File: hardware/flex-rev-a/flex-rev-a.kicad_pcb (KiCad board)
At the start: 2 copper layers, 72 x 20 mm, 51 parts, among them J601 Dock pads, SW201 button DNP, U1 ISP2454-LX, U201 nPM1304-QEAA, U401 LIS2DW12TR, U501 DRV2605LDGSR

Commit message: Lengthen both flex islands by 4 mm for a 22 x 40 mm pod
The antenna shadow on island B mirrors island A's far end across the fold,
so island A grows with island B: A is now x 96-132 (36 x 18 mm) with the
ISP2454 moved to its new far end, B is x 140-176 (36 x 20 mm). The shadow
rule area moves to x 171-176 and the 30 mm cell bay (x 140.5-170.5) ends
0.5 mm before it. Stiffener map, keep-out drawings, fab notes, layout PDF
and README pod size updated. Placement otherwise unchanged; DRC still has
no shorts, clearance, courtyard or keep-out errors (unrouted nets and
silkscreen only).

Co-Authored-By: Claude Opus 5.5 <noreply@anthropic.com>
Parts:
- moved U1 4.00 mm to (101.0, 109.0)
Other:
- board size 72 x 20 mm -> 80 x 20 mm
- board text added: "Antenna shadow after fold (x 171-176): no copper, no cell, no LRA"
- board text added: "WakeBand flex rev A, layout hand-off (step 8). Unfolded view, all parts top side. Pod about 22 x 40 mm. Island A 36 x 18, island B 36 x 20; the 30 mm cell bay ends 0.5 mm before the antenna shadow. Stackup: 2-layer adhesiveless PI 25 um, 18 um Cu, coverlay, ENIG, about 0.12 mm. Stiffeners on the bottom (User.2): FR4 0.4 under island A and the LRA pad, PI 0.2 behind the dock pads. No steel stiffen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"
- board text removed: "Antenna shadow after fold: no copper, no cell, no LRA"
- board text removed: "WakeBand flex rev A, layout hand-off (step 8). Unfolded view, all parts top side. Stackup: 2-layer adhesiveless PI 25 um, 18 um Cu, coverlay, ENIG, about 0.12 mm. Stiffeners on the bottom (User.2): FR4 0.4 under island A and the LRA pad, PI 0.2 behind the dock pads. No steel stiffeners. Bend zone (User.3): no vias or parts, R >= 1.2 mm. Vias only on stiffened areas, >= 0.5 mm from a stiffener edg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"

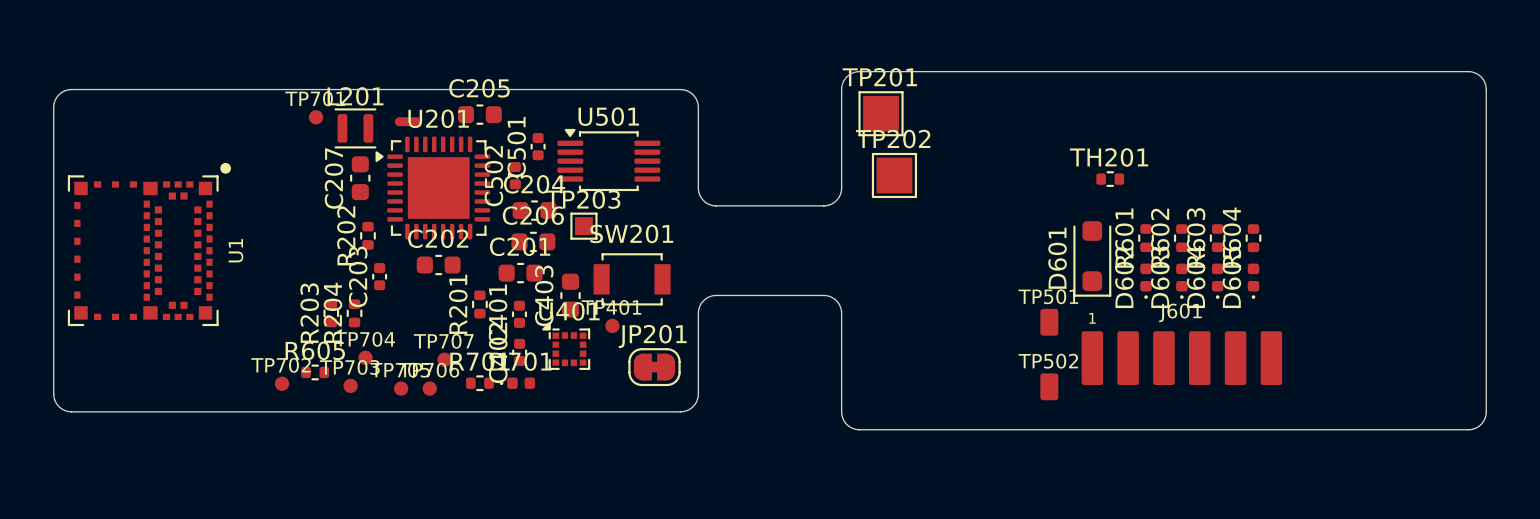
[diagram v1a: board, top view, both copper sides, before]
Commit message: Route flex rev A (partial): DRC 0 errors, 3 nets open
- Freerouting 1.9.0 route of all nets, GND included; GND pours on island A
  (both layers), island B (top) and hatched top in the neck; ISP2454 pads
  8/24 tied to 7/25; teardrops enabled on all pads and vias.
- R601-R604 moved to island A next to the neck; neck widened 5 -> 7 mm.
- Net classes (power 0.3, motor 0.25, VDD_2V0 0.2, GND 0.2, signals
  0.12 mm, clearance 0.13), no-via areas off the stiffeners, edge bands.
- DRC exclusions for the 6 ISP2454 GND pads left unconnected on purpose.
- Open: PAD_SWDIO (R602), VBUSOUT (C206), NTC (U201-TH201). Warnings are
  silkscreen only. Pad nets match the schematic; ERC still 0/0.

Co-Authored-By: Claude Opus 5.5 <noreply@anthropic.com>
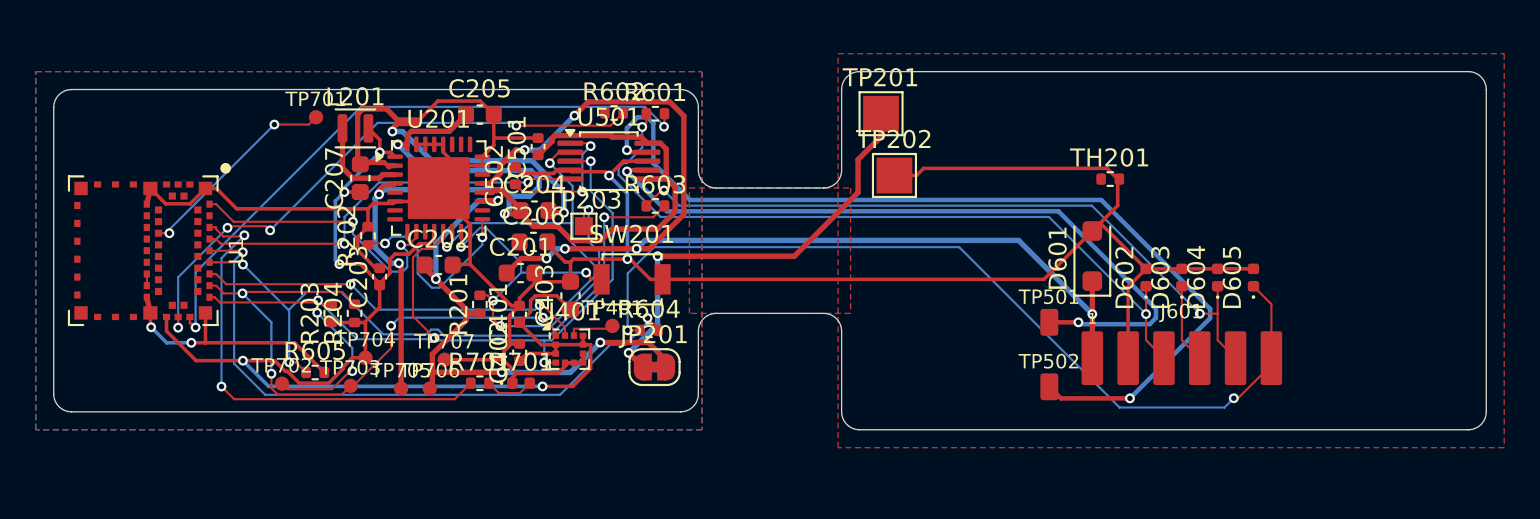
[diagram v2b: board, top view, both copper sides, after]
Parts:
- moved R604 34.1 mm to (129.2, 113.5), turned to 0 degrees
- moved R602 32.5 mm to (127.3, 101.3), turned to 0 degrees
- moved R603 31.5 mm to (129.6, 106.5), turned to 0 degrees
- moved R601 28.3 mm to (129.6, 101.3), turned to 0 degrees
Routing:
- net GND: track 0.00 -> 159.6 mm, vias 0 -> 4
- net VDD_2V0: track 0.00 -> 72.2 mm, vias 0 -> 5
- net VSYS: track 0.00 -> 64.1 mm, vias 0 -> 4
- net VIN: track 0.00 -> 62.1 mm, vias 0 -> 6
- net I2C_SCL: track 0.00 -> 54.9 mm, vias 0 -> 6
- net I2C_SDA: track 0.00 -> 52.6 mm, vias 0 -> 6
- net LRA_N: track 0.00 -> 52.6 mm, vias 0 -> 2
- net PAD_TX: track 0.00 -> 49.9 mm, vias 0 -> 2
- net PAD_SWDCLK: track 0.00 -> 41.3 mm, vias 0 -> 2
- net LRA_P: track 0.00 -> 40.5 mm, vias 0 -> 2
- net PAD_RX: track 0.00 -> 39.5 mm, vias 0 -> 2
- net UART_RX: track 0.00 -> 37.4 mm, vias 0 -> 3
- net SWDCLK: track 0.00 -> 35.1 mm, vias 0 -> 2
- net UART_TX: track 0.00 -> 35.0 mm, vias 0 -> 2
- net SWDIO: track 0.00 -> 32.4 mm, vias 0 -> 4
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- added copper zone on B.Cu, net GND
- added copper zone on F.Cu, net GND
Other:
- outline, holes or cut-outs redrawn
- board text added: "BEND (7 mm neck): no vias/parts, traces 90 deg to fold, hatched GND"
- board text removed: "BEND: no vias/parts, curved traces 90 deg to fold, hatched GND"

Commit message: Complete flex rev A routing: DRC 0 errors, 0 warnings, 0 unconnected
- Placement for routing: U501 group to the lower right of island A, U401
  group next to the module, PMIC caps regrouped so U201's power pins have a
  clear path to the neck (R601-R604 already on island A, neck 7 mm).
- Freerouting 1.9.0 for the bulk; scripted grid router for the last VSYS
  link (0.15 mm at the QFN pin) and two GND links joining module pads
  25 and 31 to the main ground.
- Neck: no vias, straight traces perpendicular to the fold, top and bottom
  traces staggered (45-degree jogs at the neck ends), hatched top GND.
- GND: solid top pours on both islands, hatched in the neck; no bottom
  pour (it only left floating slivers). No copper in the antenna keep-outs.
- ISP2454 outer-row pads only: nRESET (inner pad 13) left unrouted with
  TP701 kept; reserved GND pads 12-18, 21, 23 unconnected. 7 DRC
  exclusions with comments in the .kicad_pro.
- Teardrops enabled on all pads/vias (generated when zones are refilled in
  KiCad); reference designators moved to F.Fab, silk overlaps cleared.
- Layout PDF replotted, README routing section updated. Pad nets match the
  schematic; ERC 0/0.

Co-Authored-By: Claude Opus 5.5 <noreply@anthropic.com>
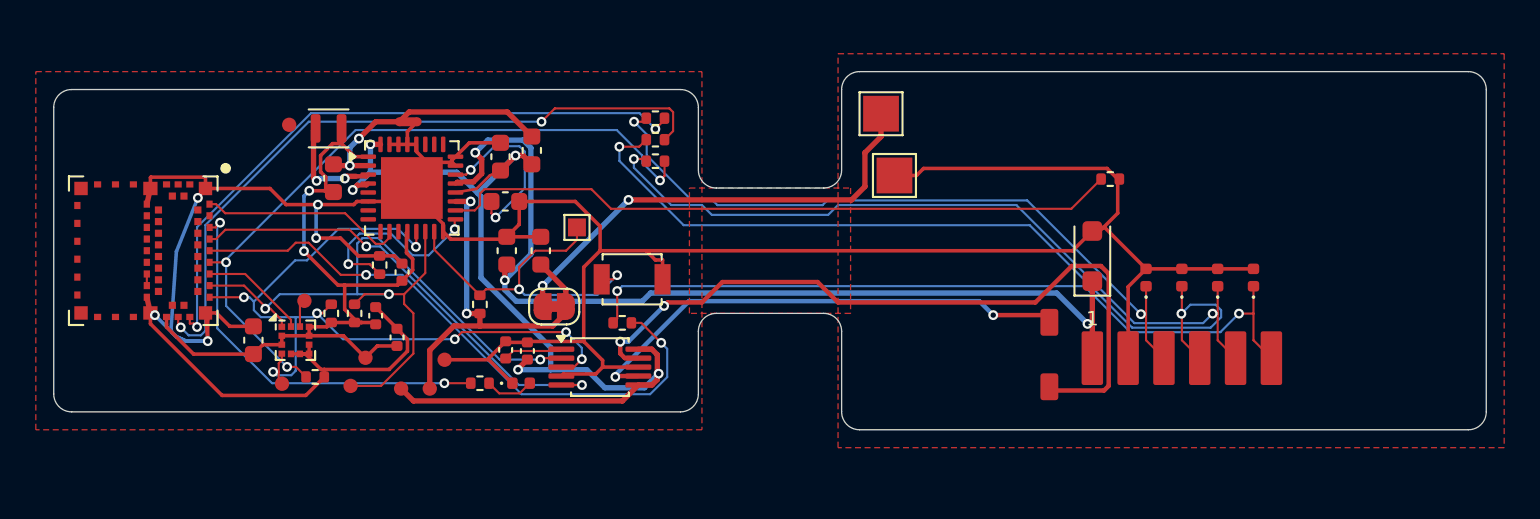
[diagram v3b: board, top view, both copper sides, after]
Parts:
- moved C403 17.9 mm to (107.2, 114.0)
- moved TP401 17.3 mm to (110.0, 111.8)
- moved U401 15.3 mm to (109.5, 114.0)
- moved U501 11.5 mm to (126.5, 115.5)
- moved C501 11.4 mm to (122.5, 114.6)
- moved C502 9.74 mm to (121.2, 114.5)
- moved C401 8.03 mm to (114.0, 112.6)
- moved C402 6.90 mm to (115.2, 113.8)
- moved JP201 6.54 mm to (124.0, 112.1)
- moved C202 5.76 mm to (123.2, 109.0), turned to 90 degrees
- moved C204 3.36 mm to (122.7, 103.4), turned to 90 degrees
- moved C206 2.75 mm to (121.2, 106.2)
- moved R602 2.75 mm to (129.6, 102.8)
- moved C205 2.62 mm to (121.0, 103.8), turned to 90 degrees
- moved R603 2.50 mm to (129.6, 104.0)
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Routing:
- net PAD_SWDIO: track 4.43 -> 47.6 mm, vias 0 -> 2
- net NTC: track 0.00 -> 38.1 mm
- net VDD_2V0: track 72.2 -> 43.1 mm, vias 5 -> 2
- net GND: track 159.6 -> 183.7 mm, vias 4 -> 5
- net ACC_INT1: track 21.8 -> 5.99 mm, vias 2 -> 0
- net LRA_P: track 40.5 -> 27.8 mm
- net nRESET: track 11.6 -> 0.00 mm, vias 2 -> 0
- net LRA_N: track 52.6 -> 41.7 mm
- net I2C_SCL: track 54.9 -> 44.5 mm, vias 6 -> 3
- net VBUSOUT: track 0.00 -> 9.99 mm, vias 0 -> 2
- net VBAT: track 31.4 -> 22.5 mm, vias 4 -> 2
- net I2C_SDA: track 52.6 -> 44.3 mm, vias 6 -> 7
- net VIN: track 62.1 -> 54.3 mm, vias 6 -> 3
- net SHPHLD: track 27.1 -> 19.8 mm, vias 5 -> 2
- net PVSS1: track 21.4 -> 14.5 mm
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- removed copper zone on B.Cu, net GND

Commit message: Fix fold orientation: cell and LRA pads to island B's B side; fab package
Island B folds under island A, so its B side is the inner face where the
cell and LRA sit.
- TP201/TP202 (cell tabs, neck end) and TP501/TP502 (LRA leads, just
  outside the LRA stiffener) moved to B.Cu/B.Mask, clear of stiffeners.
- BATT_P, LRA+, LRA- and the TP202 GND link rerouted to them; the LRA pair
  moved up on F.Cu in the neck so no trace sits over another at the fold.
- All SMT parts stay on F (single-sided assembly); NTC stays on F.
- Fold/assembly orientation note added to the fab notes layer and README.
- fab/: Gerbers (copper, mask, paste, silk, edge, bottom stiffener, bend
  zone, antenna keep-out, notes, fab) exported with --check-zones so
  teardrops are generated; Excellon drill + maps; JLCPCB BOM and top CPL
  (31 fitted parts); everything also zipped.
- DRC 0 violations / 0 unconnected / 0 footprint errors (documented
  exclusions for the reserved ISP2454 pads and nRESET); pad nets match the
  schematic; ERC 0/0.

Co-Authored-By: Claude Opus 5.5 <noreply@anthropic.com>
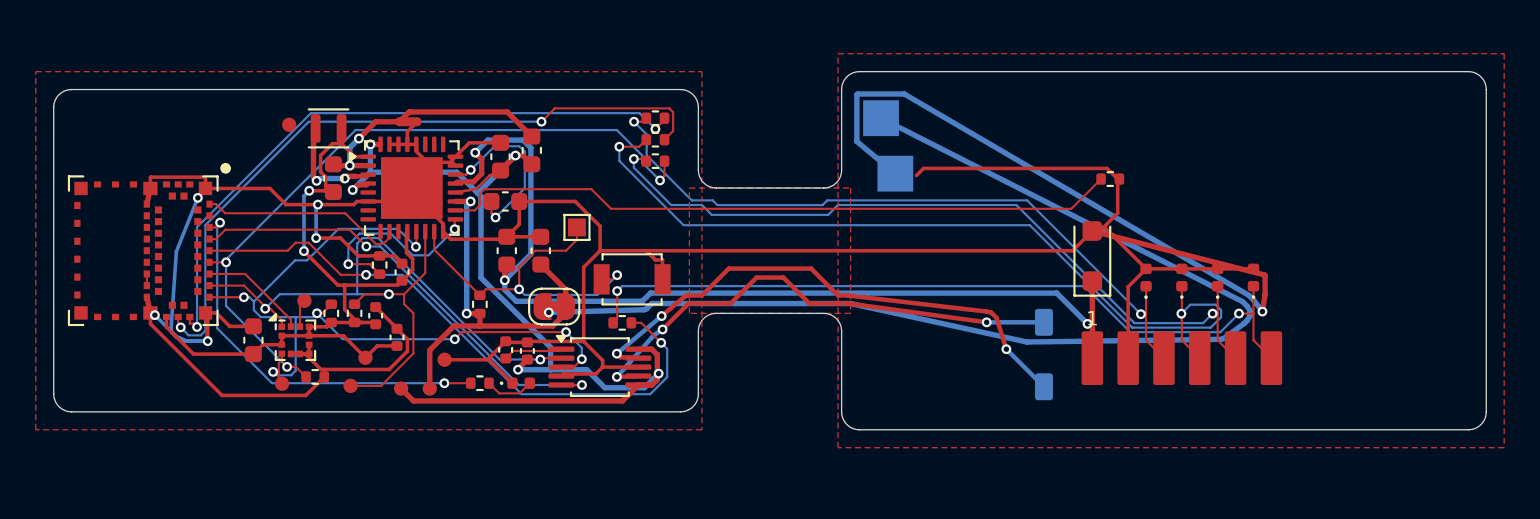
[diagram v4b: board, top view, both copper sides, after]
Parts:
- TP201, TP202, TP501, TP502: moved to B.Cu
- moved TP501 0.30 mm to (151.3, 113.0), turned to 180 degrees
- moved TP502 0.30 mm to (151.3, 116.6), turned to 180 degrees
- moved TP201 0.25 mm to (142.2, 101.6), turned to 180 degrees
- moved TP202 0.11 mm to (143.0, 104.7), turned to 180 degrees
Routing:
- net GND: track 183.7 -> 226.0 mm, vias 5 -> 6
- net BATT_P: track 25.9 -> 63.6 mm, vias 2 -> 1
- net LRA_N: track 41.7 -> 29.9 mm, vias 2 -> 3
- net LRA_P: track 27.8 -> 28.1 mm, vias 2 -> 3
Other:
- board text added: "FOLD / ASSEMBLY ORIENTATION (fold line x = 136, island B folds UNDER island A): - Island A F side (all SMT parts) faces UP, away from the wrist. - Island B F side faces DOWN to the case floor: dock pads J601 face the dock. - Cell and LRA mount on island B's B side (inner face, between the islands): cell tabs solder to TP201 (+) / TP202 (-), LRA leads to TP501 (+) / TP502 (-), all on B.Cu; LRA tap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"

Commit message: Rework flex layout per layout review: 23.5 x 40 pod, straight neck lanes
- Islands widened to 21.5 mm (pod about 23.5 x 40 mm); island B across the
  width: 0.3 edge, 12 mm cell bay, 0.5 gap, 8 mm LRA strip, 0.7 edge, so the
  LRA no longer overlaps the cell.
- Neck widened to 9 mm; every trace in it is one straight locked lane along
  x (7 on F.Cu, 4 on B.Cu), no vias, >= 0.5 mm in y between F and B lanes.
- Cell tabs TP201/TP202 and LRA leads TP501/TP502 on island B's B side,
  outside the cell bay, 0.5 mm clearance to other nets, mask +0.1 mm;
  battery +/- run 0.4 mm straight to their lanes (no vias on island B), 4
  battery-path vias on island A each doubled.
- One merged FR4 0.4 stiffener under island B's LRA/dock strip (TVS, NTC,
  dock pads on it) with windows around the B-side pads; antenna keep-out
  widened to the full island width.
- No vias on SMD pads (except 4 intended vias in the nPM1304 exposed pad);
  nRESET left unrouted (inner pad 13); ANT_LINK a 0.65 mm trace.
- GND: top pour on both islands, bottom pour on island A, hatched top in
  the neck, 24 stitching vias, solid connection on ISP2454 pads 1/7/25/31.
- Stackup: polyimide dielectric, 18 um copper, polyimide coverlay, ENIG.
- DRC 0 violations / 0 unconnected / 0 footprint errors (7 documented
  exclusions); pad nets match the schematic; ERC 0/0.

Co-Authored-By: Claude Opus 5.5 <noreply@anthropic.com>
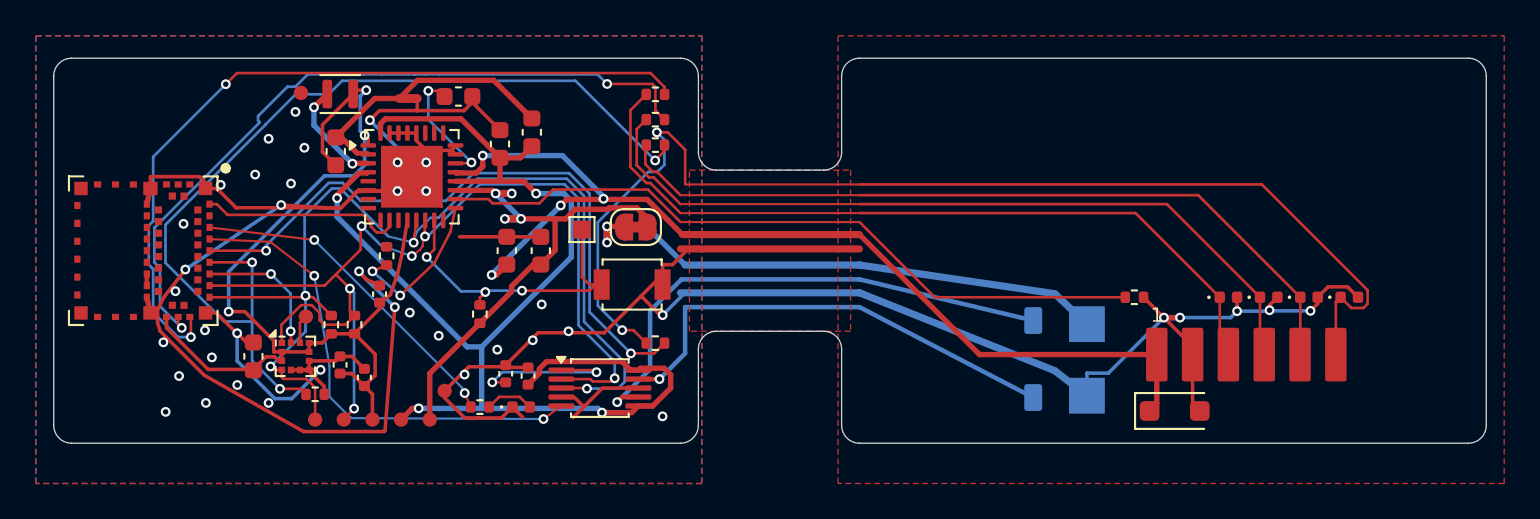
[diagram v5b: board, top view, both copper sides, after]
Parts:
- moved TP202 16.4 mm to (153.7, 117.1)
- moved TP201 16.3 mm to (153.7, 113.1)
- moved D601 9.80 mm to (158.6, 118.0), turned to 0 degrees
- moved TH201 6.74 mm to (156.3, 111.6)
- moved C206 6.42 mm to (118.6, 100.4)
- moved JP201 6.36 mm to (128.5, 107.7)
- moved D605 5.46 mm to (168.3, 111.6), turned to 0 degrees
- moved D604 5.22 mm to (166.1, 111.6), turned to 0 degrees
- moved D603 4.97 mm to (163.8, 111.6), turned to 0 degrees
- moved D602 4.73 mm to (161.6, 111.6), turned to 0 degrees
- moved J601 3.61 mm to (162.6, 114.8)
- moved TP704 3.47 mm to (113.8, 118.4)
- moved C401 3.39 mm to (112.0, 115.4)
- moved C402 2.89 mm to (113.3, 116.1)
- moved TP702 2.72 mm to (110.6, 118.4)
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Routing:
- net BATT_P: track 63.6 -> 31.3 mm, vias 1 -> 2
- net PAD_TX: track 43.4 -> 65.7 mm
- net GND: track 226.0 -> 206.6 mm, vias 6 -> 41
- net VSYS: track 57.9 -> 72.5 mm, vias 5 -> 4
- net I2C_SDA: track 44.3 -> 58.6 mm, vias 7 -> 4
- net UART_RX: track 39.4 -> 53.6 mm
- net I2C_SCL: track 44.5 -> 57.9 mm, vias 3 -> 6
- net VDD_2V0: track 43.1 -> 55.8 mm, vias 2 -> 3
- net SWDCLK: track 35.8 -> 43.9 mm
- net VBAT: track 22.5 -> 30.3 mm, vias 2 -> 4
- net REG: track 3.33 -> 8.81 mm, vias 0 -> 2
- net PAD_SWDCLK: track 39.1 -> 43.7 mm, vias 2 -> 0
- net PAD_SWDIO: track 47.6 -> 43.9 mm, vias 2 -> 0
- net LRA_N: track 29.9 -> 26.5 mm, vias 3 -> 1
- net LED_DBG: track 22.1 -> 18.7 mm
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- added copper zone on B.Cu, net GND
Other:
- board size 80 x 20 mm -> 80 x 21.5 mm
- board text added: "Antenna keep-out (module rule area + full width)"
- board text added: "BEND (9 mm neck): no vias/parts, straight traces along x only, hatched GND"
- board text added: "CELL 12 x 30 (island B, B side)"
- board text added: "FR4 0.4 (LRA + dock strip, windows at B-side pads)"
- board text added: "LRA 8 mm (B side)"
- board text added: "WakeBand flex rev A, layout hand-off. Unfolded view, all SMT parts top side. Pod about 23.5 x 40 mm. Islands 36 x 21.5 mm; the 30 mm cell bay ends 0.5 mm before the antenna shadow. Stackup: 2-layer adhesiveless PI 25 um, 18 um Cu, coverlay, ENIG, about 0.12 mm. Stiffeners on the bottom (User.2): FR4 0.4 under island A and under island B's LRA / dock strip (windows >= 0.3 mm around the B-side pads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"
- board text removed: "Antenna keep-out (module rule area)"
- board text removed: "BEND (7 mm neck): no vias/parts, traces 90 deg to fold, hatched GND"
- board text removed: "CELL 12 x 30 (inner face, under island B)"
- board text removed: "FR4 0.4 LRA"
- board text removed: "LRA 8 mm"
- board text removed: "PI 0.2 dock"
- board text removed: "WakeBand flex rev A, layout hand-off (step 8). Unfolded view, all parts top side. Pod about 22 x 40 mm. Island A 36 x 18, island B 36 x 20; the 30 mm cell bay ends 0.5 mm before the antenna shadow. Stackup: 2-layer adhesiveless PI 25 um, 18 um Cu, coverlay, ENIG, about 0.12 mm. Stiffeners on the bottom (User.2): FR4 0.4 under island A and the LRA pad, PI 0.2 behind the dock pads. No steel stiffen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"
